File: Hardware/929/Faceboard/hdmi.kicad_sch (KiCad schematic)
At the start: 1 part, among them J1 HDMI Molex 46765-2301

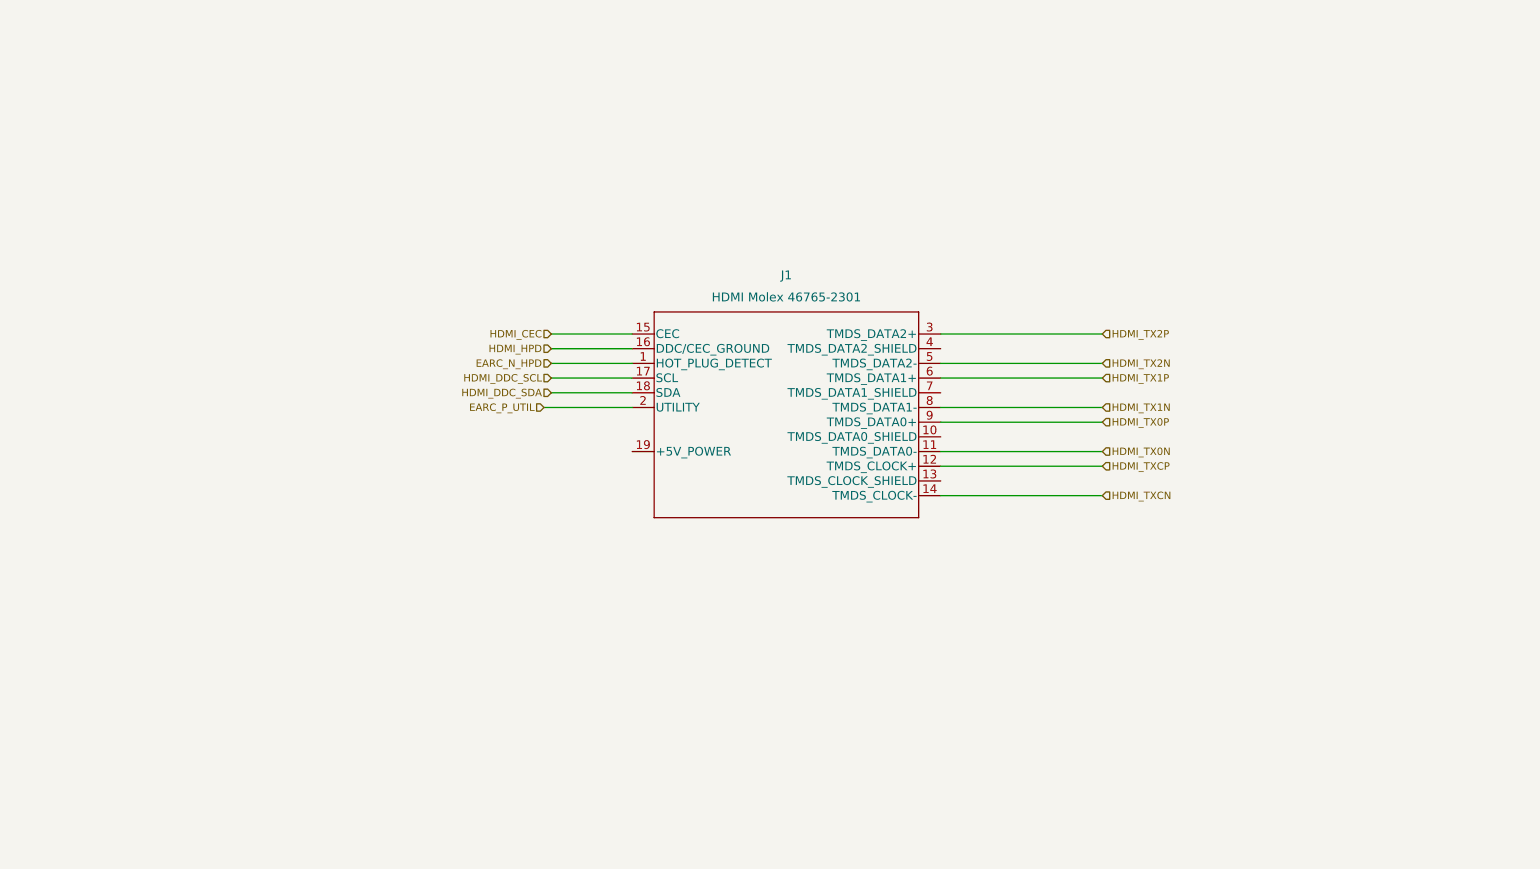
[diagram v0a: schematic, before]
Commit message: Added components
ESD HDMI
Extra components planned
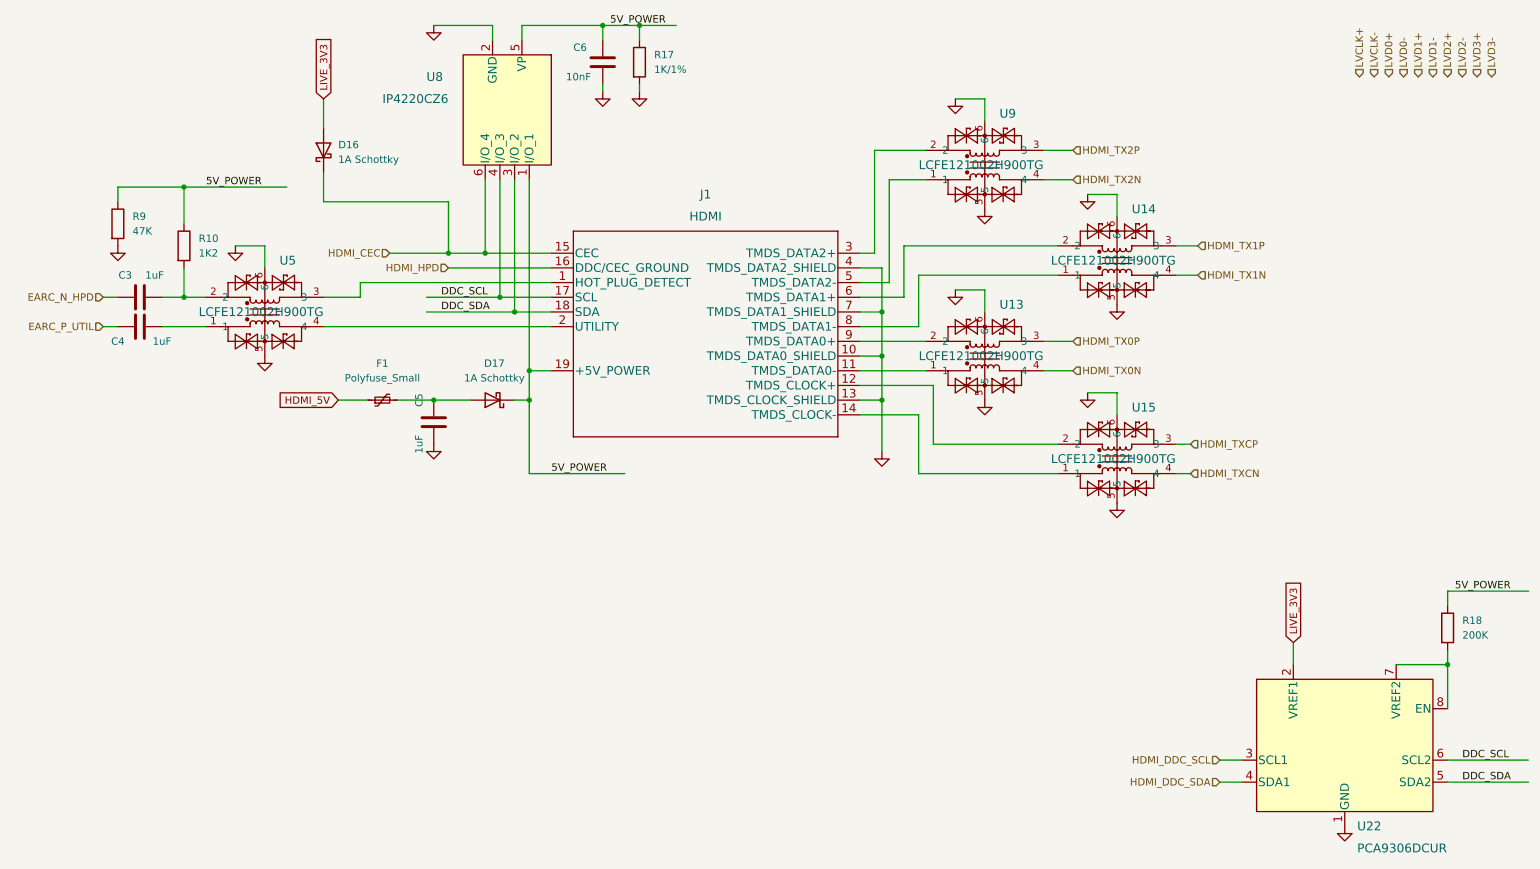
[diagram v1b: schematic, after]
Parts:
- added C3, C4, C5: 1uF, Capacitor_SMD:C_0402_1005Metric, symbol Device:C
- added C6: 10nF, Capacitor_SMD:C_0402_1005Metric, symbol Device:C
- added D16, D17: 1A Schottky, Diode_SMD:D_SOD-123F, symbol Device:D_Schottky
- added F1: Polyfuse_Small, Fuse:Fuse_0402_1005Metric, symbol Device:Polyfuse_Small
- added R10: 1K2, Resistor_SMD:R_0402_1005Metric, symbol Device:R
- added R17: 1K/1%, Resistor_SMD:R_0402_1005Metric, symbol Device:R
- added R18: 200K, Resistor_SMD:R_0402_1005Metric, symbol Device:R
- added R9: 47K, Resistor_SMD:R_0402_1005Metric, symbol Device:R
- added U13, U14, U15, U5, U9: LCFE121002H900TG, Ziloo:LCFE121002H900TG, symbol Ziloo:LCFE121002H900TG
- added U22: PCA9306DCUR, Ziloo:PCA9306DCUR, symbol Ziloo:PCA9306DCUR
- added U8: IP4220CZ6, Ziloo:IP4220CZ6, symbol Ziloo:IP4220CZ6
- J1: value HDMI Molex 46765-2301 -> HDMI; footprint 46765-2301_MOL -> Ziloo:467652301
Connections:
- net EARC_N_HPD: now also C3.1; no longer J1.1 (HOT_PLUG_DETECT)
- net EARC_P_UTIL: now also C4.1; no longer J1.2 (UTILITY)
- net HDMI_CEC: now also D16.1 (K), U8.6 (I/O_4)
- net HDMI_DDC_SCL: now also U22.3 (SCL1); no longer J1.17 (SCL)
- net HDMI_DDC_SDA: now also U22.4 (SDA1); no longer J1.18 (SDA)
- net HDMI_TX0N: now also U13.4; no longer J1.11 (TMDS_DATA0-)
- net HDMI_TX0P: now also U13.3; no longer J1.9 (TMDS_DATA0+)
- net HDMI_TX1N: now also U14.4; no longer J1.8 (TMDS_DATA1-)
- net HDMI_TX1P: now also U14.3; no longer J1.6 (TMDS_DATA1+)
- net HDMI_TX2N: now also U9.4; no longer J1.5 (TMDS_DATA2-)
- net HDMI_TX2P: now also U9.3; no longer J1.3 (TMDS_DATA2+)
- net HDMI_TXCN: now also U15.4; no longer J1.14 (TMDS_CLOCK-)
- net HDMI_TXCP: now also U15.3; no longer J1.12 (TMDS_CLOCK+)
- net GND: now reaches J1.10 (TMDS_DATA0_SHIELD)
- net GND: now also J1.13 (TMDS_CLOCK_SHIELD), J1.4 (TMDS_DATA2_SHIELD), J1.7 (TMDS_DATA1_SHIELD), C5.2, C6.2, R17.2, R9.2, U13.5, U13.6, U14.5, U14.6, U15.5, U15.6, U22.1 (GND), U5.5, U5.6, U8.2 (GND), U9.5, U9.6
- net 5V_POWER: now reaches J1.19 (+5V_POWER)
- net 5V_POWER: now also C6.1, D17.1 (K), R10.1, R17.1, R18.1, R9.1, U8.1 (I/O_1), U8.5 (VP)
- new net: J1.14 (TMDS_CLOCK-), U15.1
- new net: J1.12 (TMDS_CLOCK+), U15.2
- new net: J1.1 (HOT_PLUG_DETECT), U5.3
- new net: J1.11 (TMDS_DATA0-), U13.1
- new net: J1.2 (UTILITY), U5.4
- new net: J1.3 (TMDS_DATA2+), U9.2
- new net: J1.5 (TMDS_DATA2-), U9.1
- new net: J1.6 (TMDS_DATA1+), U14.2
- new net: J1.8 (TMDS_DATA1-), U14.1
- new net: J1.9 (TMDS_DATA0+), U13.2
- new net: C5.1, D17.2 (A), F1.2
- new net: C3.2, R10.2, U5.2
- new net: R18.2, U22.7 (VREF2), U22.8 (EN)
- new net: C4.2, U5.1
- new net DDC_SCL: J1.17 (SCL), U22.6 (SCL2), U8.4 (I/O_3)
- new net DDC_SDA: J1.18 (SDA), U22.5 (SDA2), U8.3 (I/O_2)
- new net HDMI_5V: F1.1
- new net LIVE_3V3: D16.2 (A), U22.2 (VREF1)
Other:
- moved on the sheet: J1
